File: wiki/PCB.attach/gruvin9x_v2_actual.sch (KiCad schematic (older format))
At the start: 141 parts, among them P1 CONN_5X2, P2 CONN_5, P3 CONN_6, P4 CONN_9, P5 CONN_9, P6 CONN_6, P7 CONN_12, P8 CONN_30, Q1 2SC9014, SW1 SW_PUSH, SW2 SW_PUSH, SW3 SW_PUSH, SW4 SW_PUSH, SW5 SW_PUSH, SW6 SW_PUSH, U1 78L05, U2 4066, U3 LN-6206-30, X1 16MHz

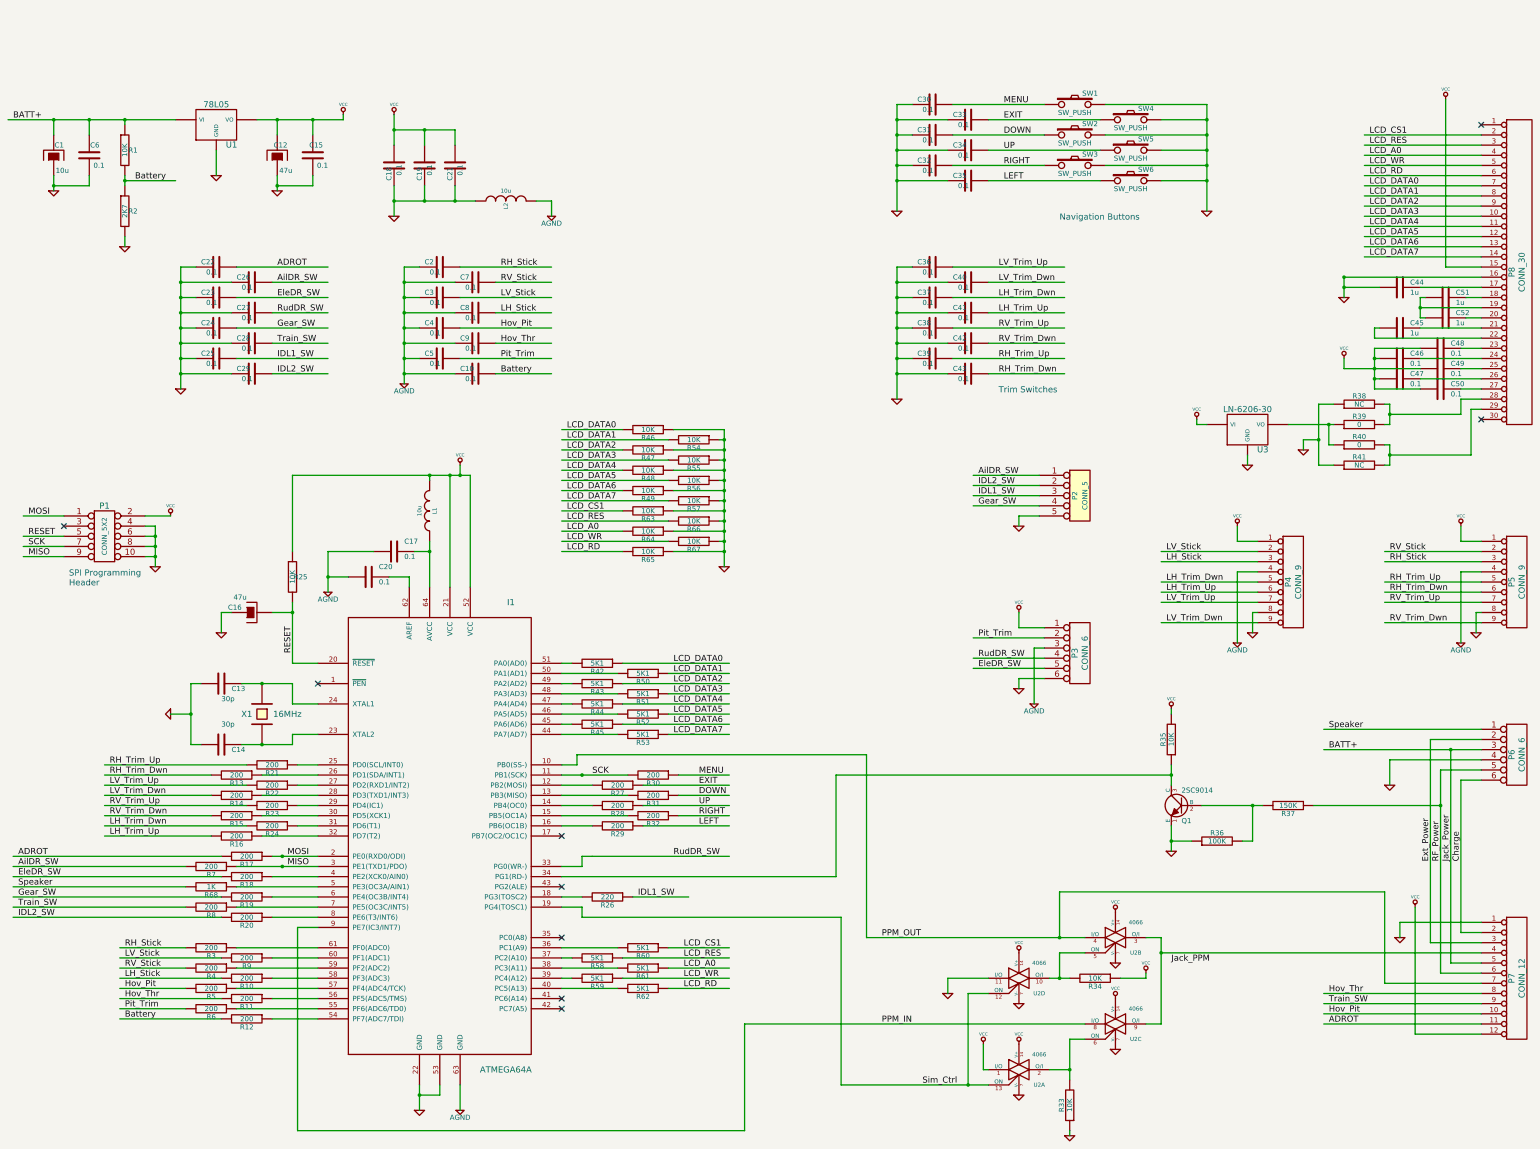
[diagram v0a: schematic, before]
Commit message: Mysterious ADROT net name changed to TCut_SW
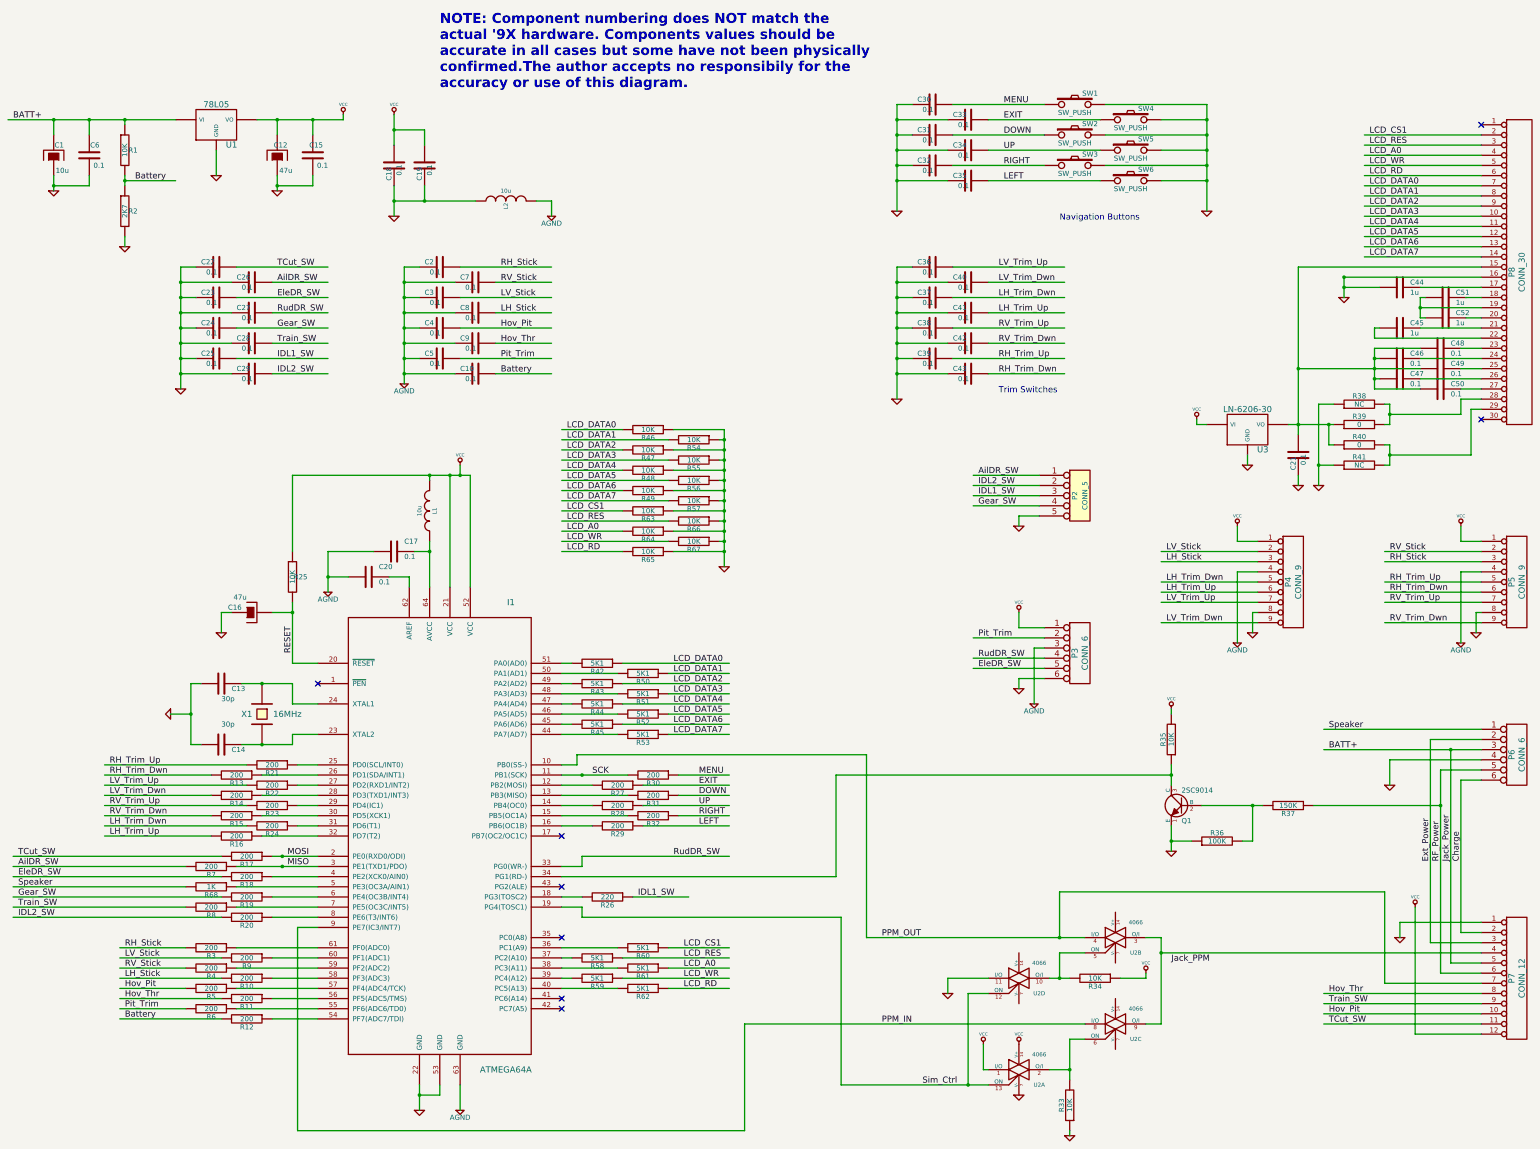
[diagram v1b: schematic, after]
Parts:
- removed P1: CONN_5X2, symbol CONN_5X2
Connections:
- net labels added: TCut_SW
- net labels removed: ADROT
- wire segments 525 -> 418
- no-connect marks 9 -> 8
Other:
- note added: "NOTE: Component numbering does NOT match the\nactual '9X hardware. Components values should be\naccurate in all cases but some have not been physically\nconfirmed.The author accepts no responsibily for the\naccuracy or use of this diagram."
- note removed: "SPI Programming\nHeader"
- moved on the sheet: C21

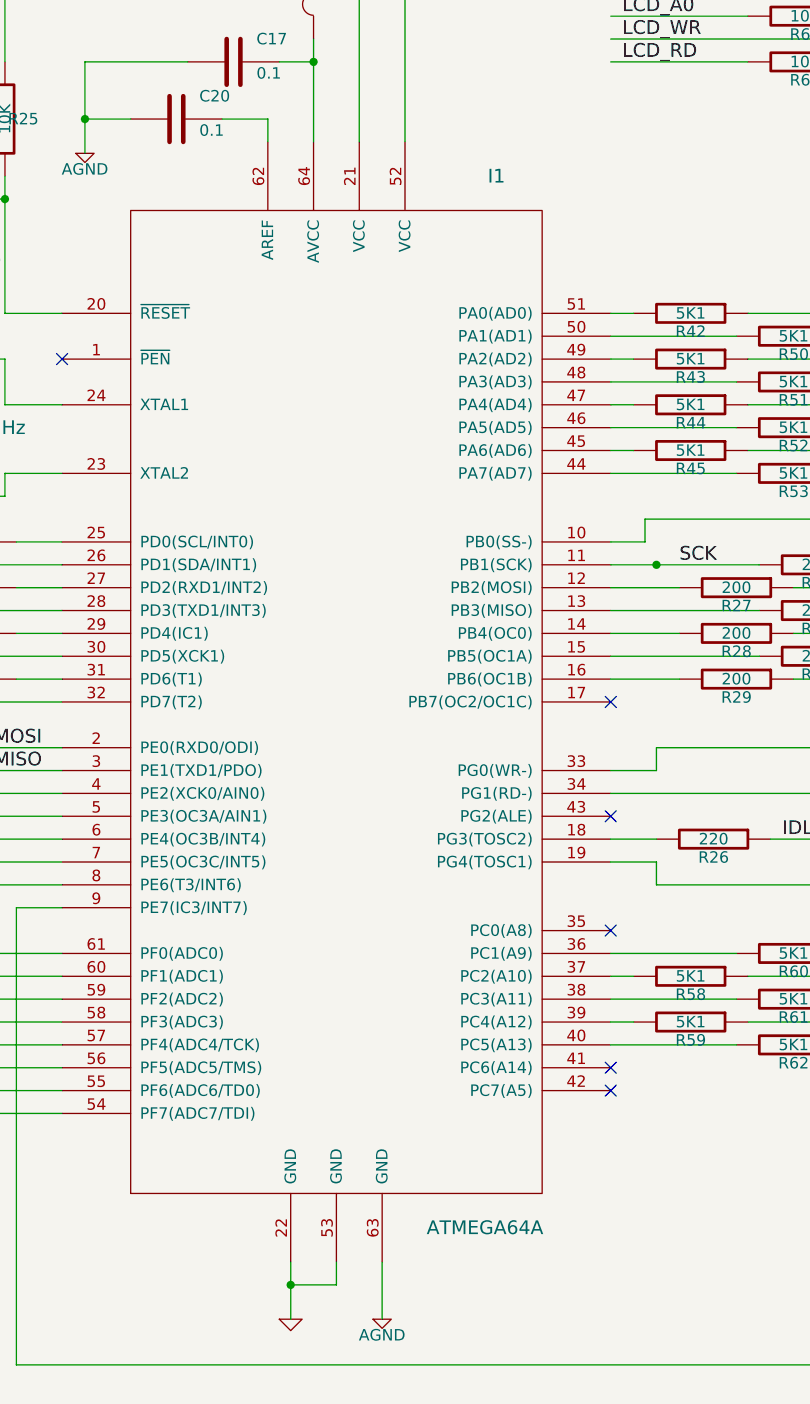
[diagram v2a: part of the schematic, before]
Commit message: Suplimentary files to make the ATmega64A part show up in the schematic. Should probably put these three in a ZIP together, instead and change the wiki link. But too tired.
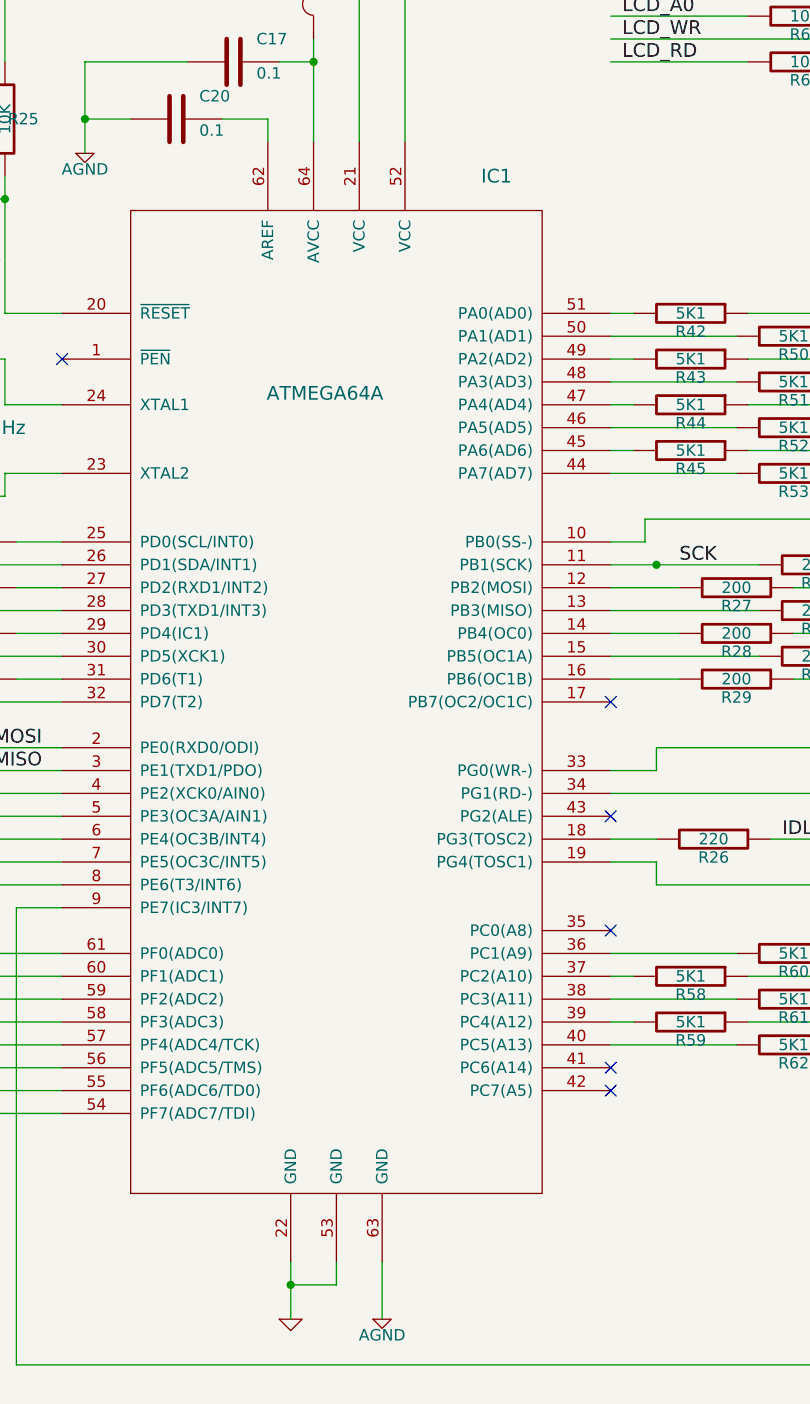
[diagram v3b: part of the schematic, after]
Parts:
- removed I1: ATMEGA64A, symbol ATMEGA64
- added IC1: ATMEGA64A, symbol ATMEGA64_GRUVIN
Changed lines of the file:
@@
-EESchema Schematic File Version 2  date 25/11/2010 7:00:05 p.m.
+EESchema Schematic File Version 2  date Mon 06 May 2013 09:57:27 PM NZST
 LIBS:power
 LIBS:device
@@
 LIBS:contrib
 LIBS:valves
-LIBS:gruvin9x_v2_actual-cache
-EELAYER 24  0
+LIBS:gruvin
+EELAYER 25  0
 EELAYER END
 $Descr A3 16535 11700
+encoding utf-8
 Sheet 1 1
 Title "Main Controller PCB (Stock)"
-Date "25 nov 2010"
+Date "6 may 2013"
 Rev "1.1"
 Comp "gruvin9x"
@@
 Comment4 ""
 $EndDescr
+$Comp
+L ATMEGA64_GRUVIN IC1
+U 1 1 51877DDF
+P 4850 8000
+F 0 "IC1" H 5550 10300 60  0000 C CNN
+F 1 "ATMEGA64A" H 4800 9350 60  0000 C CNN
+	1    4850 8000
+	1    0    0    -1
+$EndComp
 Wire Wire Line
 	13300 4450 13300 4550
@@
 	0    1    1    0
 $EndComp
-$Comp
-L ATMEGA64 I1
-U 1 1 4CE70A3F
-P 4850 8000
-F 0 "I1" H 5550 10300 60  0000 C CNN
-F 1 "ATMEGA64A" H 5500 5700 60  0000 C CNN
-	1    4850 8000
-	1    0    0    -1
-$EndComp
 $EndSCHEMATC
